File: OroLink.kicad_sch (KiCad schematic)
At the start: 11 parts, among them J10 67996-408HLF, J7 10129378-902003BLF

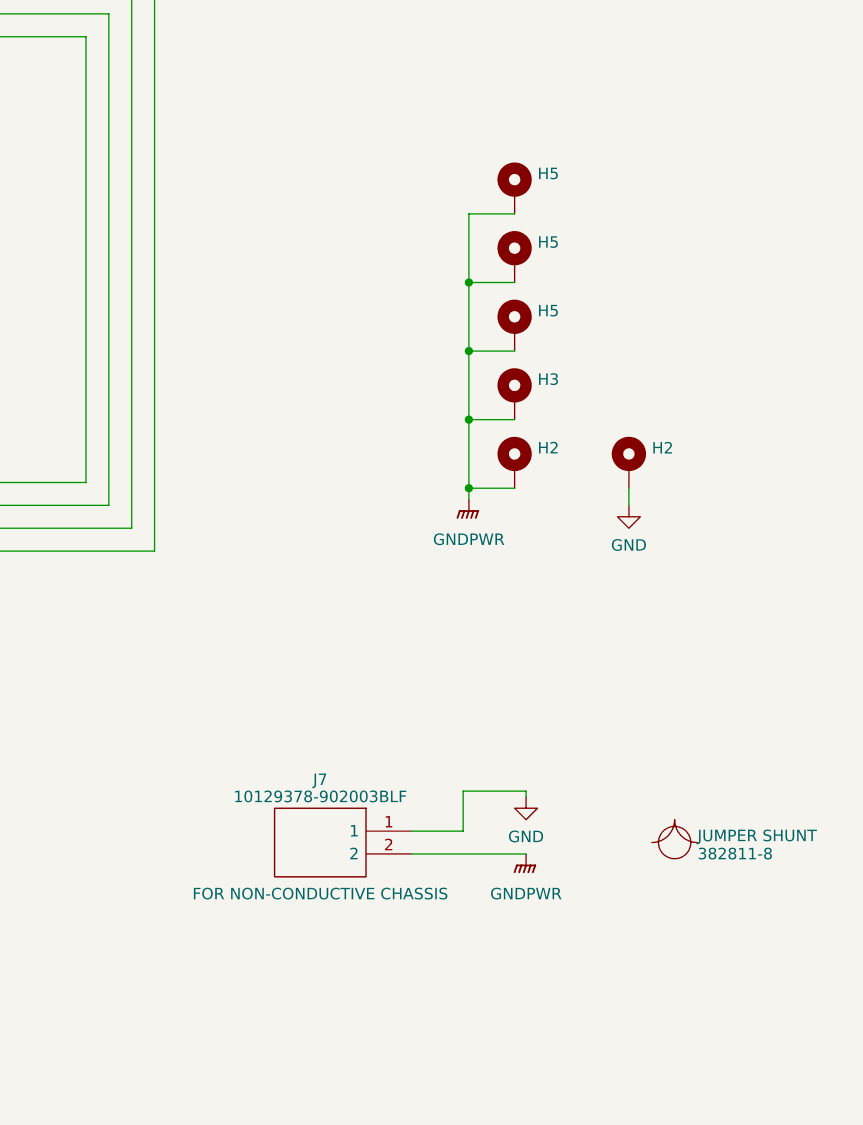
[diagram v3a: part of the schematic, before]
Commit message: remove GNDPWR jumper
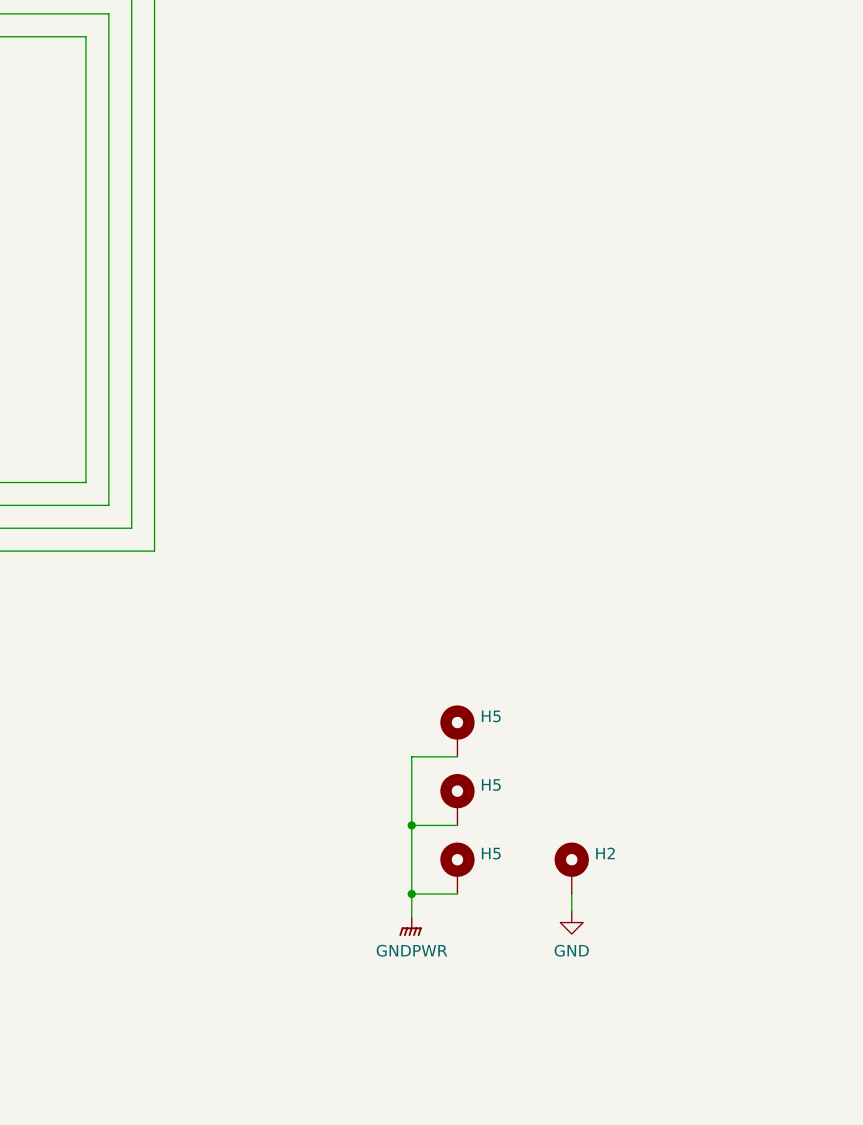
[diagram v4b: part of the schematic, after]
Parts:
- removed B2: 382811-8, symbol Oro:BOM Part
- removed H2, H3: MountingHole_Pad, MountingHole:MountingHole_3.2mm_M3_Pad_Via, symbol Mechanical:MountingHole_Pad
- removed J7: 10129378-902003BLF, HDRV2W67P0X254_1X2_508X241X1082P, symbol SamacSys_Parts:10129378-902003BLF
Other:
- moved on the sheet: H2, H5

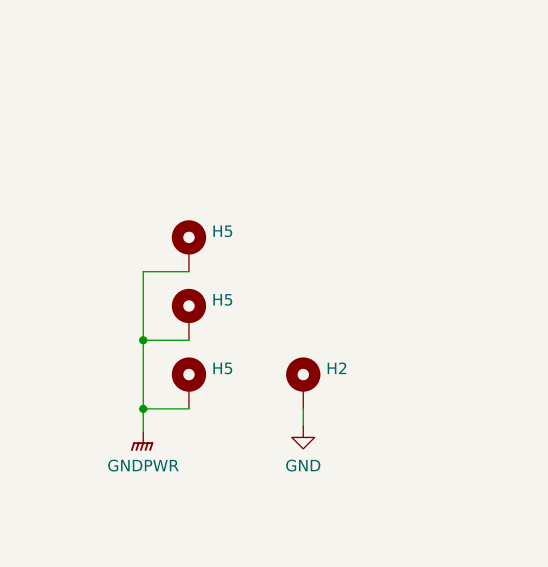
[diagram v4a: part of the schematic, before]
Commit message: fix resistor part numbers for ethernet lines
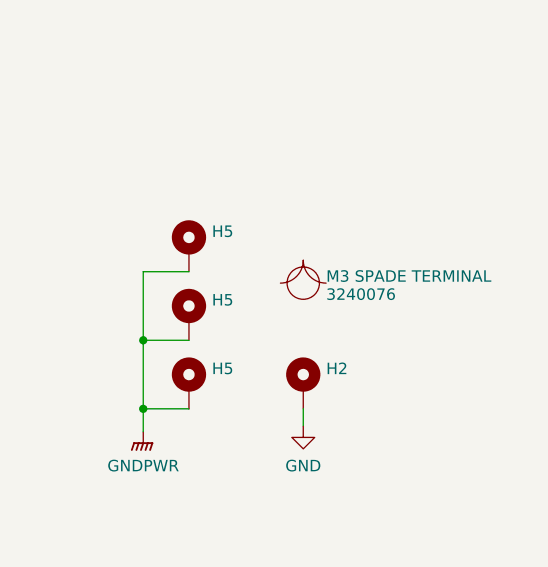
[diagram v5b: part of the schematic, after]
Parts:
- added B2: 3240076, symbol Oro:BOM Part
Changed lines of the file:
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@@
+    )
+  )
+  (symbol (lib_id "Oro:BOM Part") (at 240.03 121.92 0) (unit 1)
+    (in_bom yes) (on_board no) (dnp no)
+    (property "Reference" "B2" (at 241.935 121.2763 0)
+      (effects (font (size 1.27 1.27)) (justify left) hide)
+    )
+    (property "Value" "3240076" (at 242.57 123.19 0)
+      (effects (font (size 1.27 1.27)) (justify left))
+    )
+    (property "Footprint" "" (at 240.03 121.92 0)
+      (effects (font (size 1.27 1.27)) hide)
+    )
+    (property "Datasheet" "https://www.phoenixcontact.com/en-us/products/ring-cable-lug-c-rc-25-m3-din-3240076?type=pdf" (at 240.03 121.92 0)
+      (effects (font (size 1.27 1.27)) hide)
+    )
+    (property "Sim.Enable" "0" (at 240.03 121.92 0)
+      (effects (font (size 1.27 1.27)) hide)
+    )
+    (property "Manufacturer_Part_Number" "3240076" (at 240.03 121.92 0)
+      (effects (font (size 1.27 1.27)) hide)
+    )
+    (property "Mouser Part Number" "651-3240076" (at 240.03 121.92 0)
+      (effects (font (size 1.27 1.27)) hide)
+    )
+    (property "Note" "M3 SPADE TERMINAL" (at 242.57 121.92 0)
+      (effects (font (size 1.27 1.27)) (justify left bottom))
+    )
+    (property "BOM Qty" "8" (at 240.03 121.92 0)
+      (effects (font (size 1.27 1.27)) hide)
+    )
+    (instances
+      (project "Oro Testbed v2"
+        (path "/3d0fc623-63eb-45e5-a304-e470d9b3a173"
+          (reference "B2") (unit 1)
+        )
+        (path "/3d0fc623-63eb-45e5-a304-e470d9b3a173/7310340d-2c15-4c32-b17d-f4923dae9f8e"
+          (reference "B2") (unit 1)
+        )
+      )
+      (project "OroLink"
+        (path "/e89dcd22-1250-4a5b-b778-1c95a0dd623d/1b3eede1-74b0-4c0b-b4f1-7ec1bfc1f54f"
+          (reference "B3") (unit 1)
+        )
+        (path "/e89dcd22-1250-4a5b-b778-1c95a0dd623d"
+          (reference "B4") (unit 1)
+        )
+      )
     )
   )

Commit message: re-annotate board
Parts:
- renumbered D14 to D1, D15 to D2, J10 to J1
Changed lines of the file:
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@@
   (symbol (lib_id "SamacSys_Parts:ESDS302DBVR") (at 30.48 57.785 0) (unit 1)
     (in_bom yes) (on_board yes) (dnp no)
-    (property "Reference" "D15" (at 44.45 52.2859 0)
+    (property "Reference" "D2" (at 44.45 52.2859 0)
       (effects (font (size 1.27 1.27)))
     )
@@
       (project "OroLink"
         (path "/e89dcd22-1250-4a5b-b778-1c95a0dd623d"
-          (reference "D15") (unit 1)
+          (reference "D2") (unit 1)
         )
       )
@@
   (symbol (lib_id "power:GNDPWR") (at 222.25 138.43 0) (unit 1)
     (in_bom yes) (on_board yes) (dnp no)
-    (property "Reference" "#PWR01" (at 222.25 143.51 0)
+    (property "Reference" "#PWR02" (at 222.25 143.51 0)
       (effects (font (size 1.27 1.27)) hide)
     )
@@
       (project "OroLink"
         (path "/e89dcd22-1250-4a5b-b778-1c95a0dd623d"
-          (reference "#PWR01") (unit 1)
+          (reference "#PWR02") (unit 1)
         )
         (path "/e89dcd22-1250-4a5b-b778-1c95a0dd623d/f955395e-bf1a-4ef3-9cfe-ec9d49f66988"
@@
         )
         (path "/e89dcd22-1250-4a5b-b778-1c95a0dd623d"
-          (reference "#PWR02") (unit 1)
+          (reference "#PWR03") (unit 1)
         )
       )
@@
   (symbol (lib_id "SamacSys_Parts:ESDS302DBVR") (at 30.48 42.545 0) (unit 1)
     (in_bom yes) (on_board yes) (dnp no)
-    (property "Reference" "D14" (at 44.45 37.0459 0)
+    (property "Reference" "D1" (at 44.45 37.0459 0)
       (effects (font (size 1.27 1.27)))
     )
@@
       (project "OroLink"
         (path "/e89dcd22-1250-4a5b-b778-1c95a0dd623d"
-          (reference "D14") (unit 1)
+          (reference "D1") (unit 1)
         )
       )
@@
       (project "OroLink"
         (path "/e89dcd22-1250-4a5b-b778-1c95a0dd623d"
-          (reference "H6") (unit 1)
+          (reference "H4") (unit 1)
         )
         (path "/e89dcd22-1250-4a5b-b778-1c95a0dd623d/f955395e-bf1a-4ef3-9cfe-ec9d49f66988"
@@
         )
         (path "/e89dcd22-1250-4a5b-b778-1c95a0dd623d"
-          (reference "B4") (unit 1)
+          (reference "B1") (unit 1)
         )
       )
@@
   (symbol (lib_id "power:GNDPWR") (at 26.035 64.77 0) (mirror y) (unit 1)
     (in_bom yes) (on_board yes) (dnp no) (fields_autoplaced)
-    (property "Reference" "#PWR021" (at 26.035 69.85 0)
+    (property "Reference" "#PWR01" (at 26.035 69.85 0)
       (effects (font (size 1.27 1.27)) hide)
     )
@@
       (project "OroLink"
         (path "/e89dcd22-1250-4a5b-b778-1c95a0dd623d"
-          (reference "#PWR021") (unit 1)
+          (reference "#PWR01") (unit 1)
         )
       )
@@
   (symbol (lib_id "SamacSys_Parts:67996-408HLF") (at 97.155 33.02 0) (unit 1)
     (in_bom yes) (on_board yes) (dnp no) (fields_autoplaced)
-    (property "Reference" "J10" (at 107.315 27.5209 0)
+    (property "Reference" "J1" (at 107.315 27.5209 0)
       (effects (font (size 1.27 1.27)))
     )
@@
       (project "OroLink"
         (path "/e89dcd22-1250-4a5b-b778-1c95a0dd623d"
-          (reference "J10") (unit 1)
-        )
-      )
+          (reference "J1") (unit 1)
+        )
+      )
